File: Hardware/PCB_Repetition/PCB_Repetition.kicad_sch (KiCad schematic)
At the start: 46 parts, among them J1 Conn_01x03, J19 Conn_01x04, J2 XLR3, J20 Conn_01x04, J21 Conn_01x04, J3 XLR3, SW1 SW_SPST, SW2 SW_SPST, SW9 SW_DIP_x02, U2 ZXBM5210-SP, U4 PCF8575DBR

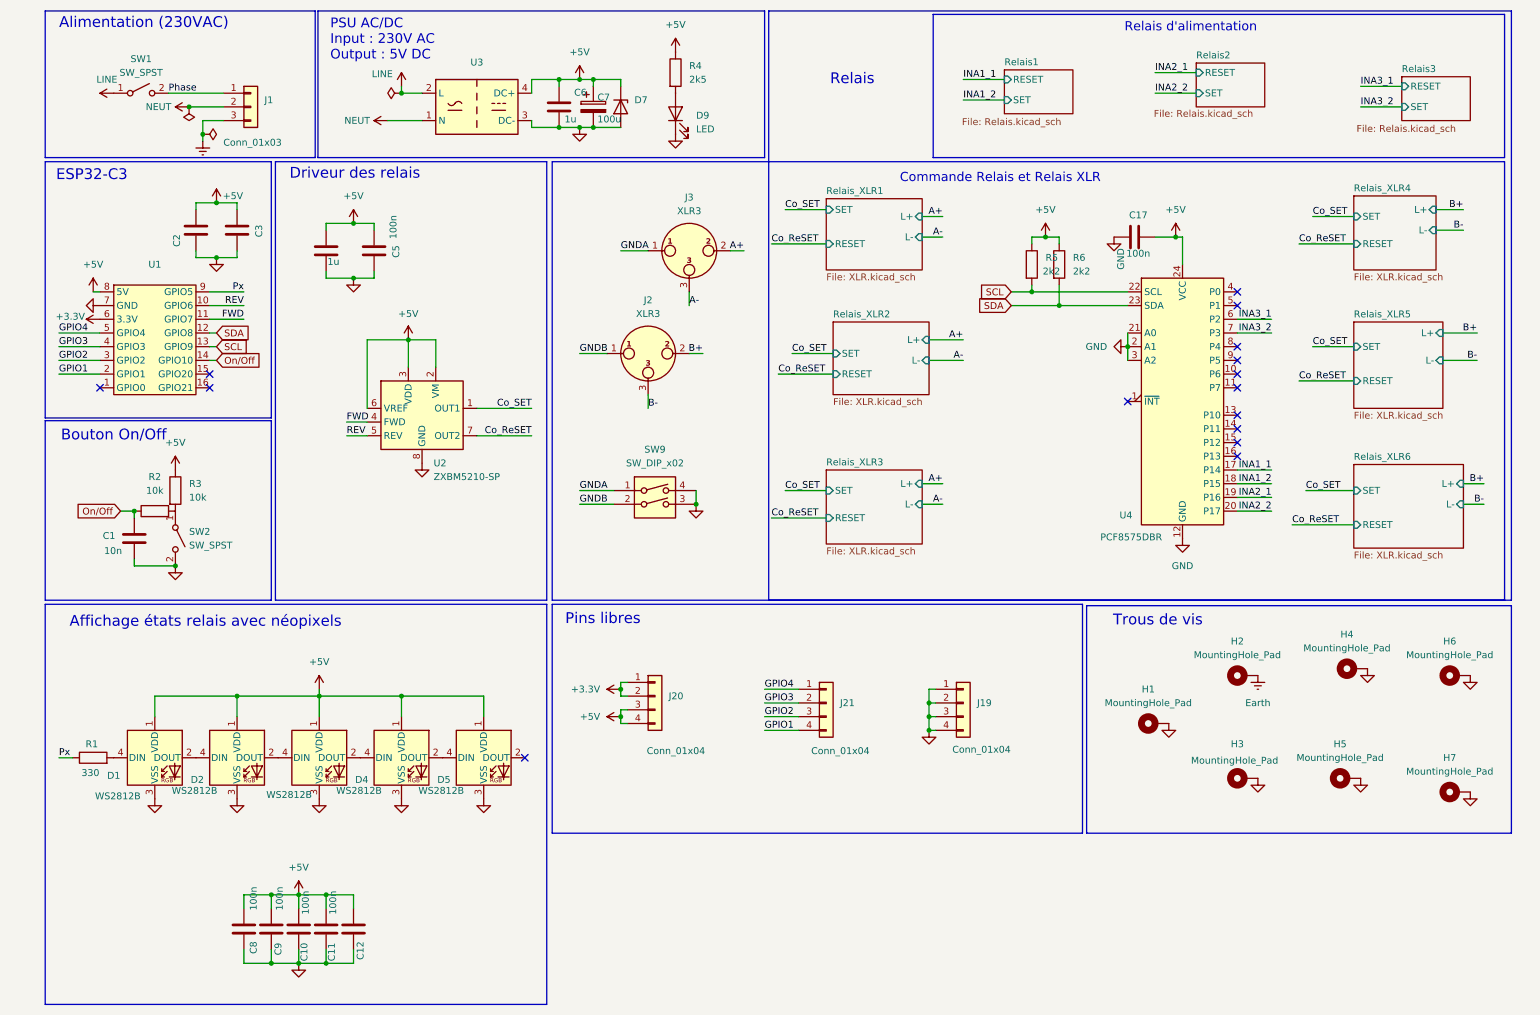
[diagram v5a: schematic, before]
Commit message: correction des pull-up sur SDA/SCL, finalisation du code esp32 Google_Calendar pour que la reconnexion (sur google device)se fasse automatiquement après reboot
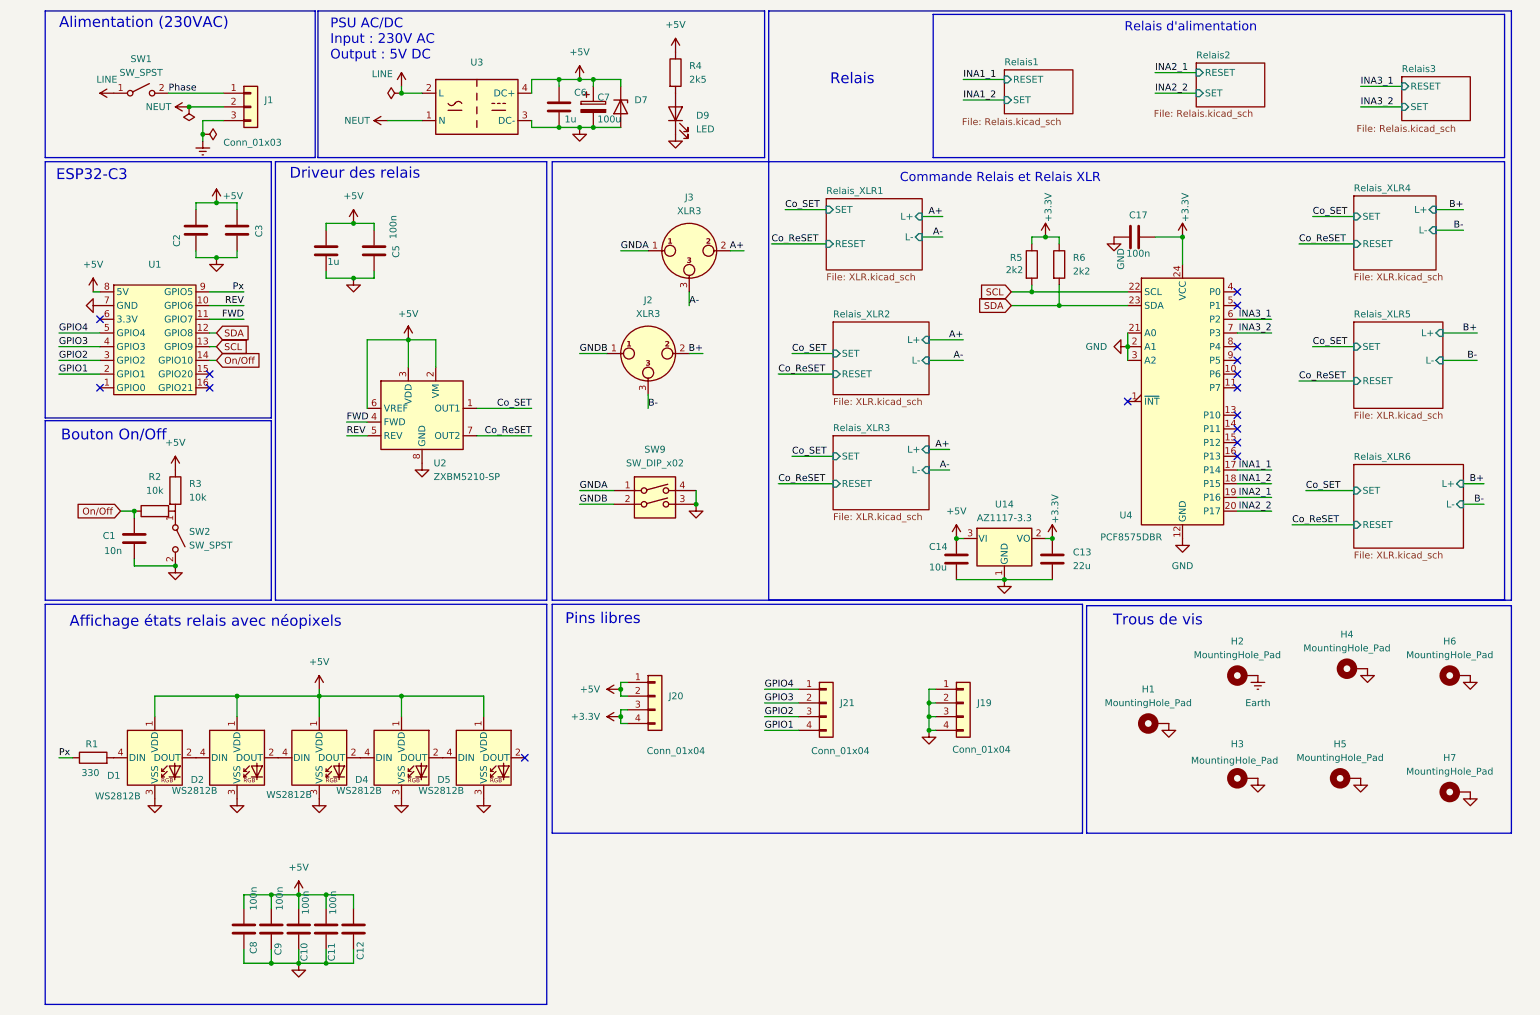
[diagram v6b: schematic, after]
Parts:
- added C13: 22u, Capacitor_SMD:C_0603_1608Metric_Pad1.08x0.95mm_HandSolder, symbol Device:C
- added C14: 10u, Capacitor_SMD:C_0603_1608Metric_Pad1.08x0.95mm_HandSolder, symbol Device:C
- added U14: AZ1117-3.3, Package_TO_SOT_SMD:SOT-223-3_TabPin2, symbol Regulator_Linear:AZ1117-3.3
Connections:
- net +3.3V: now also C17.2, J20.3 (Pin_3), J20.4 (Pin_4), R5.1, R6.1, U4.24 (VCC), C13.1, U14.2 (VO); no longer J20.1 (Pin_1), J20.2 (Pin_2), U1.6 (3.3V)
- net +5V: now also J20.1 (Pin_1), J20.2 (Pin_2), C14.1, U14.3 (VI); no longer C17.2, J20.3 (Pin_3), J20.4 (Pin_4), R5.1, R6.1, U4.24 (VCC)
- net GND: now also C13.2, C14.2, U14.1 (GND)
- no-connect marks 15 -> 16
